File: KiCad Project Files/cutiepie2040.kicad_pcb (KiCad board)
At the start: 2 copper layers, 200 x 81 mm, 105 parts, among them J1 SM04B, J2 SWD, SW1 Reset, U1 RP2040, U2 W25Q128JVS, U3 XC6206PxxxMR, Y1 12MHz

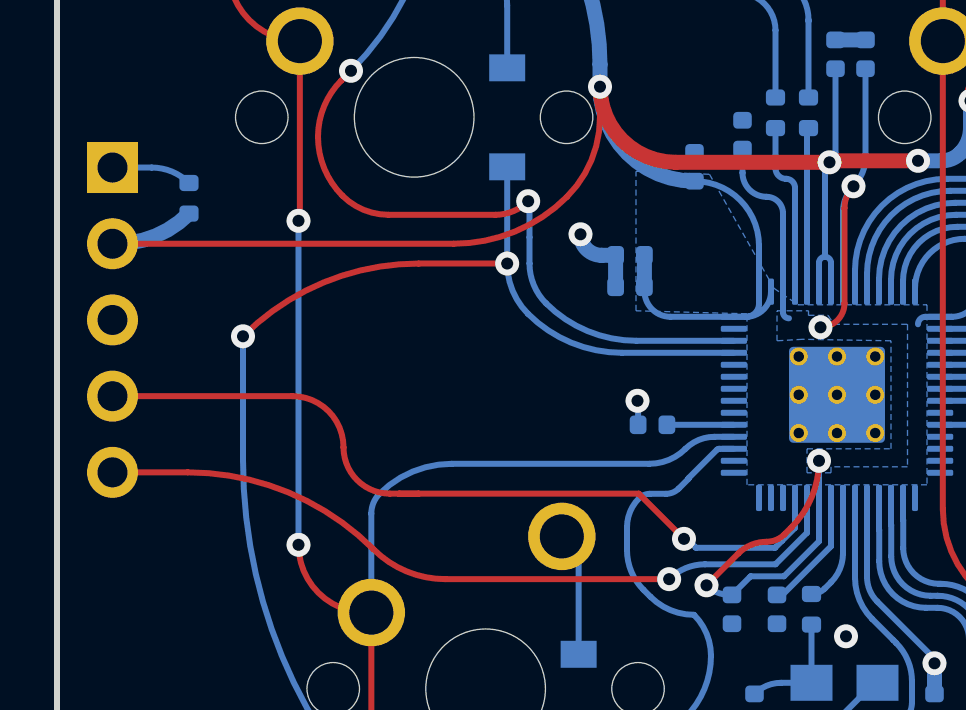
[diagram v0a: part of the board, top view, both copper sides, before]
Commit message: Create rough case, update name
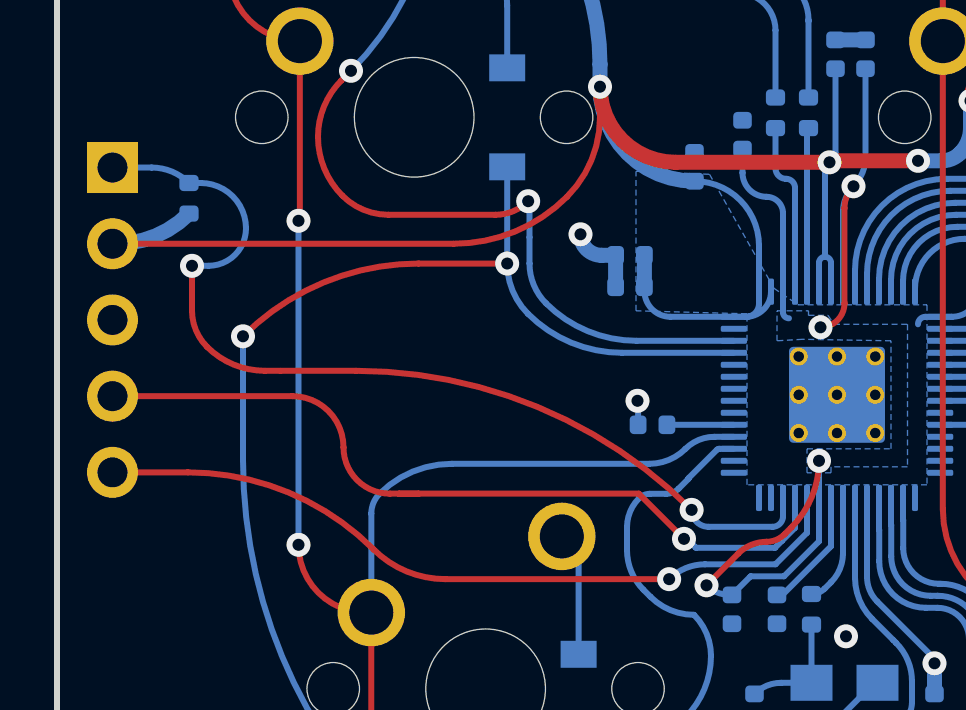
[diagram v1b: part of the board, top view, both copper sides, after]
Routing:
- net RESET: track 2.68 -> 32.3 mm, vias 0 -> 2
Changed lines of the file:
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@@
   (arc (start 63.4 65.85) (mid 63.561091 65.461091) (end 63.95 65.3) (width 0.2) (layer "B.Cu") (net 50))
   (arc (start 68.45 69.55) (mid 67.530761 69.169239) (end 67.15 68.25) (width 0.2) (layer "B.Cu") (net 50))
+  (segment (start 54.912761 82.8) (end 52.4 82.8) (width 0.2) (layer "F.Cu") (net 51))
+  (segment (start 49.45 80.792894) (end 49.45 79.3) (width 0.2) (layer "F.Cu") (net 51))
+  (segment (start 52.4 82.8) (end 51.88137 82.8) (width 0.2) (layer "F.Cu") (net 51))
+  (via (at 49.45 79.3) (size 0.8) (drill 0.4) (layers "F.Cu" "B.Cu") (net 51))
+  (via (at 66.103818 87.435488) (size 0.8) (drill 0.4) (layers "F.Cu" "B.Cu") (net 51))
+  (arc (start 49.95 82) (mid 49.579946 81.446175) (end 49.45 80.792894) (width 0.2) (layer "F.Cu") (net 51))
+  (arc (start 51.88137 82.8) (mid 50.83612 82.592087) (end 49.95 82) (width 0.2) (layer "F.Cu") (net 51))
+  (arc (start 66.103818 87.435488) (mid 60.969318 84.004724) (end 54.912761 82.8) (width 0.2) (layer "F.Cu") (net 51))
+  (segment (start 50 79.3) (end 49.45 79.3) (width 0.2) (layer "B.Cu") (net 51))
+  (segment (start 68.8 88) (end 66.66833 88) (width 0.2) (layer "B.Cu") (net 51))
+  (segment (start 49.35 76.54) (end 49.74 76.54) (width 0.2) (layer "B.Cu") (net 51))
   (segment (start 46.8 76.025) (end 48.106681 76.025) (width 0.2) (layer "B.Cu") (net 51))
+  (segment (start 69.15 87.0375) (end 69.15 87.65) (width 0.2) (layer "B.Cu") (net 51))
+  (arc (start 66.66833 88) (mid 66.26916 87.834658) (end 66.103818 87.435488) (width 0.2) (layer "B.Cu") (net 51))
+  (arc (start 51.25 78.05) (mid 50.883883 78.933883) (end 50 79.3) (width 0.2) (layer "B.Cu") (net 51))
+  (arc (start 49.74 76.54) (mid 50.807731 76.982269) (end 51.25 78.05) (width 0.2) (layer "B.Cu") (net 51))
   (arc (start 48.106681 76.025) (mid 48.77956 76.158844) (end 49.35 76.54) (width 0.2) (layer "B.Cu") (net 51))
+  (arc (start 69.15 87.65) (mid 69.047487 87.897487) (end 68.8 88) (width 0.2) (layer "B.Cu") (net 51))
   (segment (start 64.342406 86.895) (end 57.005 86.895) (width 0.2) (layer "F.Cu") (net 52))
   (segment (start 65.8495 88.402094) (end 64.342406 86.895) (width 0.2) (layer "F.Cu") (net 52))
